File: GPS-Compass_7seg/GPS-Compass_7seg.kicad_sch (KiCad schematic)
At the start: 8 parts, among them J1 1-2328702-0, U1 OSK3056A-LR, U2 MAX7219

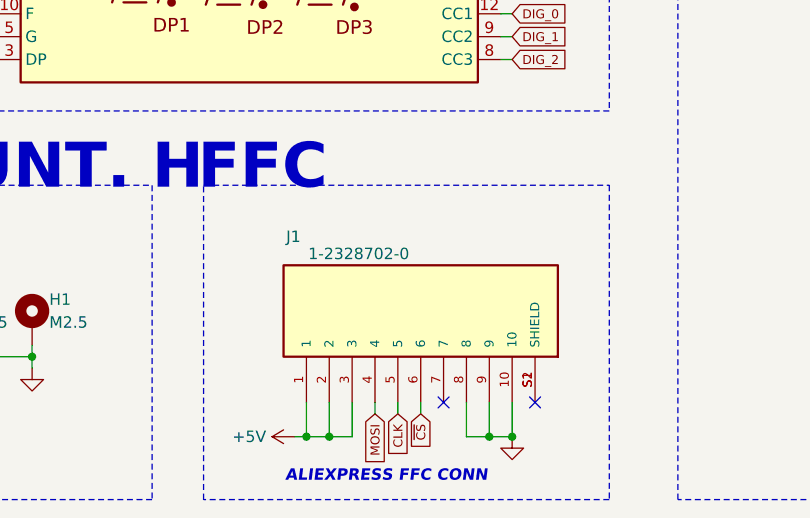
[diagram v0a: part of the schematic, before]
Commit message: UI layout and routing
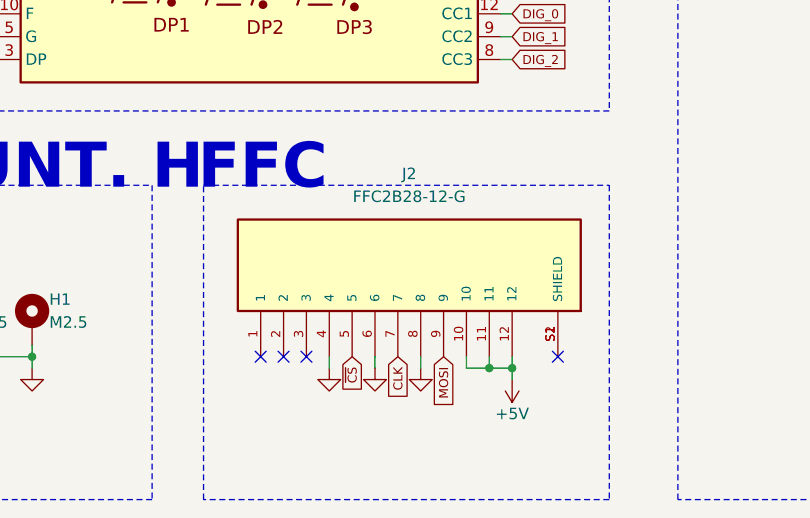
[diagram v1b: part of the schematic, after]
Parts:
- removed J1: 1-2328702-0, gps-compass_brd:TE_1-2328702-0, symbol gps-compass_sch:1-2328702-0
- added J2: FFC2B28-12-G, gps-compass_brd:GCT_FFC2B28-12-G, symbol gps-compass_sch:FFC2B28-12-G
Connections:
- net +5V: now also J2.10, J2.11, J2.12
- net CLK: now also J2.7
- net GND: now also J2.4, J2.6, J2.8
- net MOSI: now also J2.9
- net ~{CS}: now also J2.5
- new net: J2.S1 (SHIELD), J2.S2 (SHIELD)
- no-connect marks 8 -> 10
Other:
- note removed: "ALIEXPRESS FFC CONN"

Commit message: GPS Compass - schematic
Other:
- moved on the sheet: J2
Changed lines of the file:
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@@
 	)
 	(junction
-		(at 125.73 118.11)
+		(at 125.73 123.19)
 		(diameter 0)
 		(color 0 0 0 0)
 	)
 	(junction
-		(at 123.19 118.11)
+		(at 123.19 123.19)
 		(diameter 0)
 		(color 0 0 0 0)
@@
 	)
 	(no_connect
-		(at 97.79 116.84)
+		(at 97.79 121.92)
 	)
 	(no_connect
-		(at 102.87 116.84)
+		(at 102.87 121.92)
 	)
 	(no_connect
@@
 	)
 	(no_connect
-		(at 100.33 116.84)
+		(at 100.33 121.92)
 	)
 	(no_connect
@@
 	)
 	(no_connect
-		(at 130.81 116.84)
+		(at 130.81 121.92)
 	)
 	(no_connect
@@
 	(wire
 		(pts
-			(xy 125.73 118.11) (xy 123.19 118.11)
+			(xy 125.73 123.19) (xy 123.19 123.19)
 		)
 		(stroke
@@
 	(wire
 		(pts
-			(xy 123.19 118.11) (xy 123.19 116.84)
+			(xy 123.19 123.19) (xy 123.19 121.92)
 		)
 		(stroke
@@
 	(wire
 		(pts
-			(xy 110.49 116.84) (xy 110.49 118.11)
+			(xy 110.49 121.92) (xy 110.49 123.19)
 		)
 		(stroke
@@
 	(wire
 		(pts
-			(xy 125.73 119.38) (xy 125.73 118.11)
+			(xy 125.73 124.46) (xy 125.73 123.19)
 		)
 		(stroke
@@
 	(wire
 		(pts
-			(xy 125.73 118.11) (xy 125.73 116.84)
+			(xy 125.73 123.19) (xy 125.73 121.92)
 		)
 		(stroke
@@
 	(wire
 		(pts
-			(xy 115.57 116.84) (xy 115.57 118.11)
+			(xy 115.57 121.92) (xy 115.57 123.19)
 		)
 		(stroke
@@
 	(wire
 		(pts
-			(xy 123.19 118.11) (xy 120.65 118.11)
+			(xy 123.19 123.19) (xy 120.65 123.19)
 		)
 		(stroke
@@
 	(wire
 		(pts
-			(xy 120.65 118.11) (xy 120.65 116.84)
+			(xy 120.65 123.19) (xy 120.65 121.92)
 		)
 		(stroke
@@
 	(wire
 		(pts
-			(xy 105.41 116.84) (xy 105.41 118.11)
+			(xy 105.41 121.92) (xy 105.41 123.19)
 		)
 		(stroke
@@
 			"AAAAAAAAAAAAAAAAAAAAAAAAAAAAAAAAAAAAAAAAAAAAAAAAAAAAAAAAAAAAAAAAAAAAAAAAAAAA"
 			"AAAAAAAAAAAAAAAAAAAAAAAAAAAAAAAAAAAAAAAAAAAAAAAAAAAAAAAAAAAAAAAAAAAAAAAAAAAA"
+			"AAAAAAAAAAAAAAAAAAAAAAAAAAAAAAAAAAAAAAAAAAAAAAAAAAAAAAAAAAAAAAAAAAAAAAAAAAAA"
+			"AAAAAAAAAAAAAAAAAAAAAAAAAAAAAAAAAAAAAAAAAAAAAAAAAAAAAAAAAAAAAAAAAAAAAAAAAAAA"
+			"AAAAAAAAAAAAAAAAAAAAAAAAAAAAAAAAAAAAAAAAAAAAAAAAAAAAAAAAAAAAAAAAAAAAAAAAAAAA"
+			"AAAAAAAAAAAAAAAAAAAAAAAAAAAAAAAAAAAAAAAAAAAAAAAAAAAAAAAAAAAAAAAAAAAAAAAAAAAA"
+			"AAAAAAAAAAAAAAAAAAAAAAAAAAAAAAAAAAAAAAAAAAAAAAAAAAAAAAAAAAAAAAAAAAAAAAAAAAAA"
+			"AAAAAAAAAAAAAAAAAAAAAAAAAAAAAAAAAAAAAAAAAAAAAAAAAAAAAAAAAAAAAAAAAAAAAAAAAAAA"
+			"AAAAAAAAAAAAAAAAAAAAAAAAAAAAAAAAAAAAAAAAAAAAAAAAAAAAAAAAAAAAAAAAAAAAAAAAAAAA"
+			"AAAAAAAAAAAAAAAAAAAAAAAAAAAAAAAAAAAAAAAAAAAAAAAAAAAAAAAAAAAAAAAAAAAAAAAAAAAA"
+			"AAAAAAAAAAAAAAAAAAAAAAAAAAAAAAAAAAAAAAAAAAAAAAAAAAAAAAAAAAAAAAAAAAAAAAAAAAAA"
+			"AAAAAAAAAAAAAAAAAAAAAAAAAAAAAAAAAAAAAAAAAAAAAAAAAAAAAAAAAAAAAAAAAAAAAAAAAAAA"
+			"AAAAAAAAAAAAAAAAAAAAAAAAAAAAAAAAAAAAAAAAAAAAAAAAAAAAAAAAAAAAAAAAAAAAAAAAAAAA"
+			"AAAAAAAAAAAAAAAAAAAAAAAAAAAAAAAAAAAAAAAAAAAAAAAAAAAAAAAAAAAAAAAAAAAAAAAAAAAA"
+			"AAAAAAAAAAAAAAAAAAAAAAAAAAAAAAAAAAAAAAAAAAAAAAAAAAAAAAAAAAAAAAAAAAAAAAAAAAAA"
+			"AAAAAAAAAAAAAAAAAAAAAAAAAAAAAAAAAAAAAAAAAAAAAAAAAAAAAAAAAAAAAAAAAAAAAAAAAAAA"
+			"AAAAAAAAAAAAAAAAAAAAAAAAAAAAAAAAAAAAAAAAAAAAAAAAAAAAAAAAAAAAAAAAAAAAAAAAAAAA"
+			"AAAAAAAAAAAAAAAAAAAAAAAAAAAAAAAAAAAAAAAAAAAAAAAAAAAAAAAAAAAAAAAAAAAAAAAAAAAA"
+			"AAAAAAAAAAAAAAAAAAAAAAAAAAAAAAAAAAAAAAAAAAAAAAAAAAAAAAAAAAAAAAAAAAAAAAAAAAAA"
+			"AAAAAAAAAAAAAAAAAAAAAAAAAAAAAAAAAAAAAAAAAAAAAAAAAAAAAAAAAAAAAAAAAAAAAAAAAAAA"
 			"AA=="
 		)
@@
 	(global_label "MOSI"
 		(shape input)
-		(at 118.11 116.84 270)
+		(at 118.11 121.92 270)
 		(fields_autoplaced yes)
 		(effects
@@
 		)
 		(property "Intersheetrefs" "${INTERSHEET_REFS}"
-			(at 118.11 122.2148 90)
+			(at 118.11 127.2948 90)
 			(effects
 				(font
@@
 	(global_label "~{CS}"
 		(shape input)
-		(at 107.95 116.84 270)
+		(at 107.95 121.92 270)
 		(fields_autoplaced yes)
 		(effects
@@
 		)
 		(property "Intersheetrefs" "${INTERSHEET_REFS}"
-			(at 107.95 120.7152 90)
+			(at 107.95 125.7952 90)
 			(effects
 				(font
@@
 	(global_label "CLK"
 		(shape input)
-		(at 113.03 116.84 270)
+		(at 113.03 121.92 270)
 		(fields_autoplaced yes)
 		(effects
@@
 		)
 		(property "Intersheetrefs" "${INTERSHEET_REFS}"
-			(at 113.03 121.5671 90)
+			(at 113.03 126.6471 90)
 			(effects
 				(font
@@
 	(symbol
 		(lib_id "gps-compass_sch:FFC2B28-12-G")
-		(at 113.03 106.68 90)
+		(at 113.03 111.76 90)
 		(unit 1)
 		(exclude_from_sim no)
@@
 		(fields_autoplaced yes)
 		(property "Reference" "J2"
-			(at 114.3 96.52 90)
+			(at 114.3 101.6 90)
 			(effects
 				(font
@@
 		)
 		(property "Value" "FFC2B28-12-G"
-			(at 114.3 99.06 90)
+			(at 114.3 104.14 90)
 			(effects
 				(font
@@
 		)
 		(property "Footprint" "gps-compass_brd:GCT_FFC2B28-12-G"
-			(at 113.03 106.68 0)
+			(at 113.03 111.76 0)
 			(effects
 				(font
@@
 		)
 		(property "Datasheet" "https://cz.mouser.com/ProductDetail/GCT/FFC2B28-12-G?qs=KUoIvG%2F9Ilb3Lmj8zxhxfA%3D%3D"
-			(at 113.03 106.68 0)
+			(at 113.03 111.76 0)
 			(effects
 				(font
@@
 		)
 		(property "Description" ""
-			(at 113.03 106.68 0)
+			(at 113.03 111.76 0)
 			(effects
 				(font
@@
 		)
 		(property "MF" "Global Connector Technology"
-			(at 113.03 106.68 0)
+			(at 113.03 111.76 0)
 			(effects
 				(font
@@
 		)
 		(property "MAXIMUM_PACKAGE_HEIGHT" "1.75mm"
-			(at 113.03 106.68 0)
+			(at 113.03 111.76 0)
 			(effects
 				(font
@@
 		)
 		(property "Package" "None"
-			(at 113.03 106.68 0)
+			(at 113.03 111.76 0)
 			(effects
 				(font
@@
 		)
 		(property "Price" "None"
-			(at 113.03 106.68 0)
+			(at 113.03 111.76 0)
 			(effects
 				(font
@@
 		)
 		(property "Check_prices" "https://www.snapeda.com/parts/FFC2B28-12-G/Global+Connector+Technology/view-part/?ref=eda"
-			(at 113.03 106.68 0)
+			(at 113.03 111.76 0)
 			(effects
 				(font
@@
 		)
 		(property "STANDARD" "Manufacturer Recommendations"
-			(at 113.03 106.68 0)
+			(at 113.03 111.76 0)
 			(effects
 				(font
@@
 		)
 		(property "PARTREV" "A"
-			(at 113.03 106.68 0)
+			(at 113.03 111.76 0)
 			(effects
 				(font
@@
 		)
 		(property "SnapEDA_Link" "https://www.snapeda.com/parts/FFC2B28-12-G/Global+Connector+Technology/view-part/?ref=snap"
-			(at 113.03 106.68 0)
+			(at 113.03 111.76 0)
 			(effects
 				(font
@@
 		)
 		(property "MP" "FFC2B28-12-G"
-			(at 113.03 106.68 0)
+			(at 113.03 111.76 0)
 			(effects
 				(font
@@
 		)
 		(property "Description_1" "12 Position FFC, FPC Connector Contacts, Top and Bottom 0.020 (0.50mm) Surface Mount, Right Angle"
-			(at 113.03 106.68 0)
+			(at 113.03 111.76 0)
 			(effects
 				(font
@@
 		)
 		(property "Availability" "In Stock"
-			(at 113.03 106.68 0)
+			(at 113.03 111.76 0)
 			(effects
 				(font
@@
 		)
 		(property "MANUFACTURER" "GCT"
-			(at 113.03 106.68 0)
+			(at 113.03 111.76 0)
 			(effects
 				(font
@@
 	(symbol
 		(lib_id "power:GND")
-		(at 110.49 118.11 0)
+		(at 110.49 123.19 0)
 		(mirror y)
 		(unit 1)
@@
 		(fields_autoplaced yes)
 		(property "Reference" "#PWR08"
-			(at 110.49 124.46 0)
+			(at 110.49 129.54 0)
 			(effects
 				(font
@@
 		)
 		(property "Value" "GND"
-			(at 110.49 123.19 0)
+			(at 110.49 128.27 0)
 			(effects
 				(font
@@
 		)
 		(property "Footprint" ""
-			(at 110.49 118.11 0)
+			(at 110.49 123.19 0)
 			(effects
 				(font
@@
 		)
 		(property "Datasheet" ""
-			(at 110.49 118.11 0)
+			(at 110.49 123.19 0)
 			(effects
 				(font
@@
 		)
 		(property "Description" ""
-			(at 110.49 118.11 0)
+			(at 110.49 123.19 0)
 			(effects
 				(font
@@
 	(symbol
 		(lib_id "power:GND")
-		(at 115.57 118.11 0)
+		(at 115.57 123.19 0)
 		(mirror y)
 		(unit 1)
@@
 		(fields_autoplaced yes)
 		(property "Reference" "#PWR09"
-			(at 115.57 124.46 0)
+			(at 115.57 129.54 0)
 			(effects
 				(font
@@
 		)
 		(property "Value" "GND"
-			(at 115.57 123.19 0)
+			(at 115.57 128.27 0)
 			(effects
 				(font
@@
 		)
 		(property "Footprint" ""
-			(at 115.57 118.11 0)
+			(at 115.57 123.19 0)
 			(effects
 				(font
@@
 		)
 		(property "Datasheet" ""
-			(at 115.57 118.11 0)
+			(at 115.57 123.19 0)
 			(effects
 				(font
@@
 		)
 		(property "Description" ""
-			(at 115.57 118.11 0)
+			(at 115.57 123.19 0)
 			(effects
 				(font
@@
 	(symbol
 		(lib_id "power:+5V")
-		(at 125.73 119.38 180)
+		(at 125.73 124.46 180)
 		(unit 1)
 		(exclude_from_sim no)
@@
 		(dnp no)
 		(property "Reference" "#PWR03"
-			(at 125.73 115.57 0)
+			(at 125.73 120.65 0)
 			(effects
 				(font
@@
 		)
 		(property "Value" "+5V"
-			(at 125.73 123.19 0)
+			(at 125.73 128.27 0)
 			(effects
 				(font
@@
 		)
 		(property "Footprint" ""
-			(at 125.73 119.38 0)
+			(at 125.73 124.46 0)
 			(effects
 				(font
@@
 		)
 		(property "Datasheet" ""
-			(at 125.73 119.38 0)
+			(at 125.73 124.46 0)
 			(effects
 				(font
@@
 		)
 		(property "Description" "Power symbol creates a global label with name \"+5V\""
-			(at 125.73 119.38 0)
+			(at 125.73 124.46 0)
 			(effects
 				(font
@@
 	(symbol
 		(lib_id "power:GND")
-		(at 105.41 118.11 0)
+		(at 105.41 123.19 0)
 		(mirror y)
 		(unit 1)
@@
 		(fields_autoplaced yes)
 		(property "Reference" "#PWR02"
-			(at 105.41 124.46 0)
+			(at 105.41 129.54 0)
 			(effects
 				(font
@@
 		)
 		(property "Value" "GND"
-			(at 105.41 123.19 0)
+			(at 105.41 128.27 0)
 			(effects
 				(font
@@
 		)
 		(property "Footprint" ""
-			(at 105.41 118.11 0)
+			(at 105.41 123.19 0)
 			(effects
 				(font
@@
 		)
 		(property "Datasheet" ""
-			(at 105.41 118.11 0)
+			(at 105.41 123.19 0)
 			(effects
 				(font
@@
 		)
 		(property "Description" ""
-			(at 105.41 118.11 0)
+			(at 105.41 123.19 0)
 			(effects
 				(font

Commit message: changes s
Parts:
- removed C1: 10uF, Capacitor_Tantalum_SMD:CP_EIA-3216-18_Kemet-A_Pad1.58x1.35mm_HandSolder, symbol Device:C_Polarized
- added C1: 10uF, Capacitor_SMD:C_0805_2012Metric, symbol Device:C
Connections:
- net +5V: now also C1.1
- net GND: now also C1.2
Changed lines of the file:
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@@
 	(wire
 		(pts
+			(xy 118.11 128.27) (xy 118.11 121.92)
+		)
+		(stroke
+			(width 0)
+			(type default)
+		)
+	)
+	(wire
+		(pts
 			(xy 200.66 85.09) (xy 195.58 85.09)
 		)
@@
 	(wire
 		(pts
+			(xy 107.95 128.27) (xy 107.95 121.92)
+		)
+		(stroke
+			(width 0)
+			(type default)
+		)
+	)
+	(wire
+		(pts
 			(xy 123.19 123.19) (xy 123.19 121.92)
 		)
@@
 	(wire
 		(pts
+			(xy 113.03 128.27) (xy 113.03 121.92)
+		)
+		(stroke
+			(width 0)
+			(type default)
+		)
+	)
+	(wire
+		(pts
 			(xy 200.66 105.41) (xy 195.58 105.41)
 		)
@@
 		)
 	)
-	(global_label "DIG_2"
-		(shape input)
-		(at 200.66 105.41 0)
-		(fields_autoplaced yes)
+	(label "MOSI"
+		(at 118.11 128.27 90)
 		(effects
 			(font
@@
 				(color 0 0 0 1)
 			)
-			(justify left)
+			(justify left bottom)
 		)
-		(property "Intersheetrefs" "${INTERSHEET_REFS}"
-			(at 206.4012 105.41 0)
-			(effects
-				(font
-					(size 1.27 1.27)
-				)
-				(justify left)
-				(hide yes)
+	)
+	(label "~{CS}"
+		(at 107.95 128.27 90)
+		(effects
+			(font
+				(face "Bahnschrift")
+				(size 1 1)
+				(color 0 0 0 1)
 			)
+			(justify left bottom)
 		)
 	)
-	(global_label "DIG_0"
+	(label "CLK"
+		(at 113.03 128.27 90)
+		(effects
+			(font
+				(face "Bahnschrift")
+				(size 1 1)
+				(color 0 0 0 1)
+			)
+			(justify left bottom)
+		)
+	)
+	(global_label "DIG_2"
 		(shape input)
-		(at 125.73 78.74 0)
+		(at 200.66 105.41 0)
 		(fields_autoplaced yes)
 		(effects
@@
 		)
 		(property "Intersheetrefs" "${INTERSHEET_REFS}"
-			(at 131.481 78.74 0)
+			(at 206.4012 105.41 0)
 			(effects
 				(font
@@
 		)
 	)
-	(global_label "MOSI"
+	(global_label "DIG_0"
 		(shape input)
-		(at 118.11 121.92 270)
+		(at 125.73 78.74 0)
 		(fields_autoplaced yes)
 		(effects
@@
 				(color 0 0 0 1)
 			)
-			(justify right)
+			(justify left)
 		)
 		(property "Intersheetrefs" "${INTERSHEET_REFS}"
-			(at 118.11 127.2948 90)
+			(at 131.481 78.74 0)
 			(effects
 				(font
 					(size 1.27 1.27)
 				)
-				(justify right)
+				(justify left)
 				(hide yes)
 			)
@@
 		)
 	)
-	(global_label "~{CS}"
-		(shape input)
-		(at 107.95 121.92 270)
-		(fields_autoplaced yes)
-		(effects
-			(font
-				(face "Bahnschrift")
-				(size 1 1)
-				(color 0 0 0 1)
-			)
-			(justify right)
-		)
-		(property "Intersheetrefs" "${INTERSHEET_REFS}"
-			(at 107.95 125.7952 90)
-			(effects
-				(font
-					(size 1.27 1.27)
-				)
-				(justify right)
-				(hide yes)
-			)
-		)
-	)
 	(global_label "SEG_F"
 		(shape input)
@@
 		)
 	)
-	(global_label "CLK"
-		(shape input)
-		(at 113.03 121.92 270)
-		(fields_autoplaced yes)
-		(effects
-			(font
-				(face "Bahnschrift")
-				(size 1 1)
-				(color 0 0 0 1)
-			)
-			(justify right)
-		)
-		(property "Intersheetrefs" "${INTERSHEET_REFS}"
-			(at 113.03 126.6471 90)
-			(effects
-				(font
-					(size 1.27 1.27)
-				)
-				(justify right)
-				(hide yes)
-			)
-		)
-	)
 	(global_label "MOSI"
 		(shape input)
@@
 	(symbol
 		(lib_id "Device:C")
-		(at 193.04 72.39 90)
+		(at 193.04 64.77 90)
 		(mirror x)
 		(unit 1)
@@
 		(on_board yes)
 		(dnp no)
-		(property "Reference" "C2"
-			(at 198.12 74.295 90)
+		(property "Reference" "C1"
+			(at 198.12 66.675 90)
 			(effects
 				(font
@@
 			)
 		)
-		(property "Value" "100nF"
-			(at 198.12 76.2 90)
+		(property "Value" "10uF"
+			(at 198.12 68.58 90)
 			(effects
 				(font
@@
 		)
 		(property "Footprint" "Capacitor_SMD:C_0805_2012Metric"
-			(at 196.85 73.3552 0)
+			(at 196.85 65.7352 0)
 			(effects
 				(font
@@
 		)
 		(property "Datasheet" "~"
-			(at 193.04 72.39 0)
+			(at 193.04 64.77 0)
 			(effects
 				(font
@@
 		)
 		(property "Description" ""
-			(at 193.04 72.39 0)
+			(at 193.04 64.77 0)
 			(effects
 				(font
@@
 			(project "GPS-Compass_7seg"
 				(path "/4bca8f90-4150-41f0-a662-0d11f178f1b3"
-					(reference "C2")
+					(reference "C1")
 					(unit 1)
 				)
@@
 	)
 	(symbol
-		(lib_id "Mechanical:MountingHole_Pad")
-		(at 63.5 113.03 0)
+		(lib_id "Device:C")
+		(at 193.04 72.39 90)
+		(mirror x)
 		(unit 1)
 		(exclude_from_sim no)
-		(in_bom no)
+		(in_bom yes)
 		(on_board yes)
 		(dnp no)
-		(property "Reference" "H2"
-			(at 65.405 110.49 0)
+		(property "Reference" "C2"
+			(at 198.12 74.295 90)
 			(effects
 				(font
@@
 			)
 		)
-		(property "Value" "M2.5"
-			(at 65.405 113.03 0)
+		(property "Value" "100nF"
+			(at 198.12 76.2 90)
 			(effects
 				(font
@@
 			)
 		)
-		(property "Footprint" "MountingHole:MountingHole_2.7mm_M2.5_Pad_Via"
-			(at 63.5 113.03 0)
+		(property "Footprint" "Capacitor_SMD:C_0805_2012Metric"
+			(at 196.85 73.3552 0)
 			(effects
 				(font
+					(face "Bahnschrift")
 					(size 1.27 1.27)
 				)
@@
 		)
 		(property "Datasheet" "~"
-			(at 63.5 113.03 0)
+			(at 193.04 72.39 0)
 			(effects
 				(font
+					(face "Bahnschrift")
 					(size 1.27 1.27)
 				)
@@
 			)
 		)
-		(property "Description" "Mounting Hole with connection"
-			(at 63.5 113.03 0)
+		(property "Description" ""
+			(at 193.04 72.39 0)
 			(effects
 				(font
@@
 		(pin "1"
 		)
+		(pin "2"
+		)
 		(instances
 			(project "GPS-Compass_7seg"
 				(path "/4bca8f90-4150-41f0-a662-0d11f178f1b3"
-					(reference "H2")
+					(reference "C2")
 					(unit 1)
 				)
@@
 	)
 	(symbol
-		(lib_id "power:GND")
-		(at 115.57 123.19 0)
-		(mirror y)
+		(lib_id "Mechanical:MountingHole_Pad")
+		(at 63.5 113.03 0)
 		(unit 1)
 		(exclude_from_sim no)
-		(in_bom yes)
+		(in_bom no)
 		(on_board yes)
 		(dnp no)
-		(fields_autoplaced yes)
-		(property "Reference" "#PWR09"
-			(at 115.57 129.54 0)
+		(property "Reference" "H2"
+			(at 65.405 110.49 0)
 			(effects
 				(font
 					(size 1.27 1.27)
 				)
-				(hide yes)
+				(justify left)
 			)
 		)
-		(property "Value" "GND"
-			(at 115.57 128.27 0)
+		(property "Value" "M2.5"
+			(at 65.405 113.03 0)
 			(effects
 				(font
 					(size 1.27 1.27)
 				)
-				(hide yes)
+				(justify left)
 			)
 		)
-		(property "Footprint" ""
-			(at 115.57 123.19 0)
+		(property "Footprint" "MountingHole:MountingHole_2.7mm_M2.5_Pad_Via"
+			(at 63.5 113.03 0)
 			(effects
 				(font
-					(face "Bahnschrift")
 					(size 1.27 1.27)
 				)
@@
 			)
 		)
-		(property "Datasheet" ""
-			(at 115.57 123.19 0)
+		(property "Datasheet" "~"
+			(at 63.5 113.03 0)
 			(effects
 				(font
-					(face "Bahnschrift")
 					(size 1.27 1.27)
 				)
@@
 			)
 		)
-		(property "Description" ""
-			(at 115.57 123.19 0)
+		(property "Description" "Mounting Hole with connection"
+			(at 63.5 113.03 0)
 			(effects
 				(font
@@
 			(project "GPS-Compass_7seg"
 				(path "/4bca8f90-4150-41f0-a662-0d11f178f1b3"
-					(reference "#PWR09")
+					(reference "H2")
 					(unit 1)
 				)
@@
 	)
 	(symbol
-		(lib_id "Device:C_Polarized")
-		(at 193.04 64.77 90)
+		(lib_id "power:GND")
+		(at 115.57 123.19 0)
+		(mirror y)
 		(unit 1)
 		(exclude_from_sim no)
@@
 		(on_board yes)
 		(dnp no)
-		(property "Reference" "C1"
-			(at 198.12 66.675 90)
+		(fields_autoplaced yes)
+		(property "Reference" "#PWR09"
+			(at 115.57 129.54 0)
 			(effects
 				(font
 					(size 1.27 1.27)
 				)
-				(justify left)
+				(hide yes)
 			)
 		)
-		(property "Value" "10uF"
-			(at 198.12 68.58 90)
+		(property "Value" "GND"
+			(at 115.57 128.27 0)
 			(effects
 				(font
 					(size 1.27 1.27)
 				)
-				(justify left)
+				(hide yes)
 			)
 		)
-		(property "Footprint" "Capacitor_Tantalum_SMD:CP_EIA-3216-18_Kemet-A_Pad1.58x1.35mm_HandSolder"
-			(at 196.85 63.8048 0)
+		(property "Footprint" ""
+			(at 115.57 123.19 0)
 			(effects
 				(font
@@
 			)
 		)
-		(property "Datasheet" "~"
-			(at 193.04 64.77 0)
+		(property "Datasheet" ""
+			(at 115.57 123.19 0)
 			(effects
 				(font
@@
 		)
 		(property "Description" ""
-			(at 193.04 64.77 0)
+			(at 115.57 123.19 0)
 			(effects
 				(font
@@
 		(pin "1"
 		)
-		(pin "2"
-		)
 		(instances
 			(project "GPS-Compass_7seg"
 				(path "/4bca8f90-4150-41f0-a662-0d11f178f1b3"
-					(reference "C1")
+					(reference "#PWR09")
 					(unit 1)
 				)
